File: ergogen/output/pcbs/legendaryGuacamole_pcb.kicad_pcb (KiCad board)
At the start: 2 copper layers, 47 parts

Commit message: forget to commit
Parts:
- removed REF**: XIAO-nRF52840-SMD, XIAO-nRF52840-SMD
- moved S22 215.1 mm to (227.2, 149.6), turned to -40 degrees
- moved D22 214.3 mm to (224.0, 153.5), turned to -40 degrees
- moved S21 209.5 mm to (213.8, 128.7), turned to -30 degrees
- moved D21 208.8 mm to (211.3, 133.0), turned to -30 degrees
- moved S20 207.0 mm to (204.3, 145.2), turned to -30 degrees
- moved D20 206.4 mm to (201.8, 149.5), turned to -30 degrees
- moved S19 201.4 mm to (191.5, 120.1), turned to -20 degrees
- moved D19 201.0 mm to (189.8, 124.8), turned to -20 degrees
- moved S18 200.0 mm to (185.0, 138.0), turned to -20 degrees
- moved D12 200.0 mm to (176.0, 98.7)
- moved D13 200.0 mm to (176.0, 79.7)
- moved D15 200.0 mm to (195.0, 98.7)
- moved D16 200.0 mm to (195.0, 79.7)
- moved D6 200.0 mm to (138.0, 98.7)
- moved D7 200.0 mm to (138.0, 79.7)
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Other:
- net class Default removed

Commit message: final key layout
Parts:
- added D23: , ComboDiode, F.Cu at (222.1, 143.9)
- added REF**: XIAO-nRF52840-SMD, XIAO-nRF52840-SMD, F.Cu at (0.00, 0.00)
- added S23: , MX, F.Cu at (224.6, 139.6)
- moved S18 82.9 mm to (195.0, 55.7), turned to 0 degrees
- moved D18 82.9 mm to (195.0, 60.7), turned to 0 degrees
- moved D12 48.2 mm to (157.0, 54.3)
- moved S12 48.2 mm to (157.0, 49.3)
- moved D15 42.5 mm to (176.0, 60.7)
- moved S15 42.5 mm to (176.0, 55.7)
- moved D3 42.5 mm to (100.0, 67.0)
- moved S3 42.5 mm to (100.0, 62.0)
- moved D6 36.9 mm to (119.0, 67.0)
- moved S6 36.9 mm to (119.0, 62.0)
- moved D9 36.9 mm to (138.0, 60.7)
- moved S9 36.9 mm to (138.0, 55.7)
- moved S20 34.7 mm to (184.3, 116.8), turned to -10 degrees
- moved S22 34.3 mm to (207.7, 121.3), turned to -20 degrees
- moved D20 33.3 mm to (183.4, 121.7), turned to -10 degrees
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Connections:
- D10 pad 1: P7 -> P8
- D10 pad 2: middle_home -> middle_bottom
- D11 pad 1: P6 -> P7
- D11 pad 2: middle_top -> middle_home
- D12 pad 1: P8 -> P6
- D12 pad 2: index_bottom -> middle_top
- D13 pad 1: P7 -> P8
- D13 pad 2: index_home -> index_bottom
- D14 pad 1: P6 -> P7
- D14 pad 2: index_top -> index_home
- D15 pad 1: P8 -> P6
- D15 pad 2: inner_bottom -> index_top
- D16 pad 1: P7 -> P8
- D16 pad 2: inner_home -> inner_bottom
- D17 pad 1: P6 -> P7
- D17 pad 2: inner_top -> inner_home
- D18 pad 1: P10 -> P6
- D18 pad 2: thumb_1_row_0 -> inner_top
- D19 pad 1: P9 -> P10
- D19 pad 2: thumb_1_row_1 -> thumb_1_row_0
- D20 pad 1: P10 -> P9
- D20 pad 2: thumb_2_row_0 -> thumb_1_row_1
- D21 pad 1: P9 -> P10
- D21 pad 2: thumb_2_row_1 -> thumb_2_row_0
- D22 pad 1: P10 -> P9
- D22 pad 2: thumb_3_row_0 -> thumb_2_row_1
- D3 pad 1: P8 -> P6
- D3 pad 2: pinky_bottom -> outer_top
- D4 pad 1: P7 -> P8
- D4 pad 2: pinky_home -> pinky_bottom
- D5 pad 1: P6 -> P7
- D5 pad 2: pinky_top -> pinky_home
- D6 pad 1: P8 -> P6
- D6 pad 2: ring_bottom -> pinky_top
- D7 pad 1: P7 -> P8
- D7 pad 2: ring_home -> ring_bottom
- D8 pad 1: P6 -> P7
- D8 pad 2: ring_top -> ring_home
- D9 pad 1: P8 -> P6
- D9 pad 2: middle_bottom -> ring_top
- S10 pad 2: middle_home -> middle_bottom
- S11 pad 2: middle_top -> middle_home
- S12 pad 1: P4 -> P3
- S12 pad 2: index_bottom -> middle_top
- S13 pad 2: index_home -> index_bottom
- S14 pad 2: index_top -> index_home
- S15 pad 1: P5 -> P4
- S15 pad 2: inner_bottom -> index_top
- S16 pad 2: inner_home -> inner_bottom
- S17 pad 2: inner_top -> inner_home
- S18 pad 1: P3 -> P5
- S18 pad 2: thumb_1_row_0 -> inner_top
- S19 pad 2: thumb_1_row_1 -> thumb_1_row_0
- S20 pad 1: P4 -> P3
- S20 pad 2: thumb_2_row_0 -> thumb_1_row_1
- S21 pad 2: thumb_2_row_1 -> thumb_2_row_0
- S22 pad 1: P5 -> P4
- S22 pad 2: thumb_3_row_0 -> thumb_2_row_1
- S3 pad 1: P1 -> P0
- S3 pad 2: pinky_bottom -> outer_top
- S4 pad 2: pinky_home -> pinky_bottom
- S5 pad 2: pinky_top -> pinky_home
- S6 pad 1: P2 -> P1
- S6 pad 2: ring_bottom -> pinky_top
- S7 pad 2: ring_home -> ring_bottom
- S8 pad 2: ring_top -> ring_home
- S9 pad 1: P3 -> P2
- S9 pad 2: middle_bottom -> ring_top

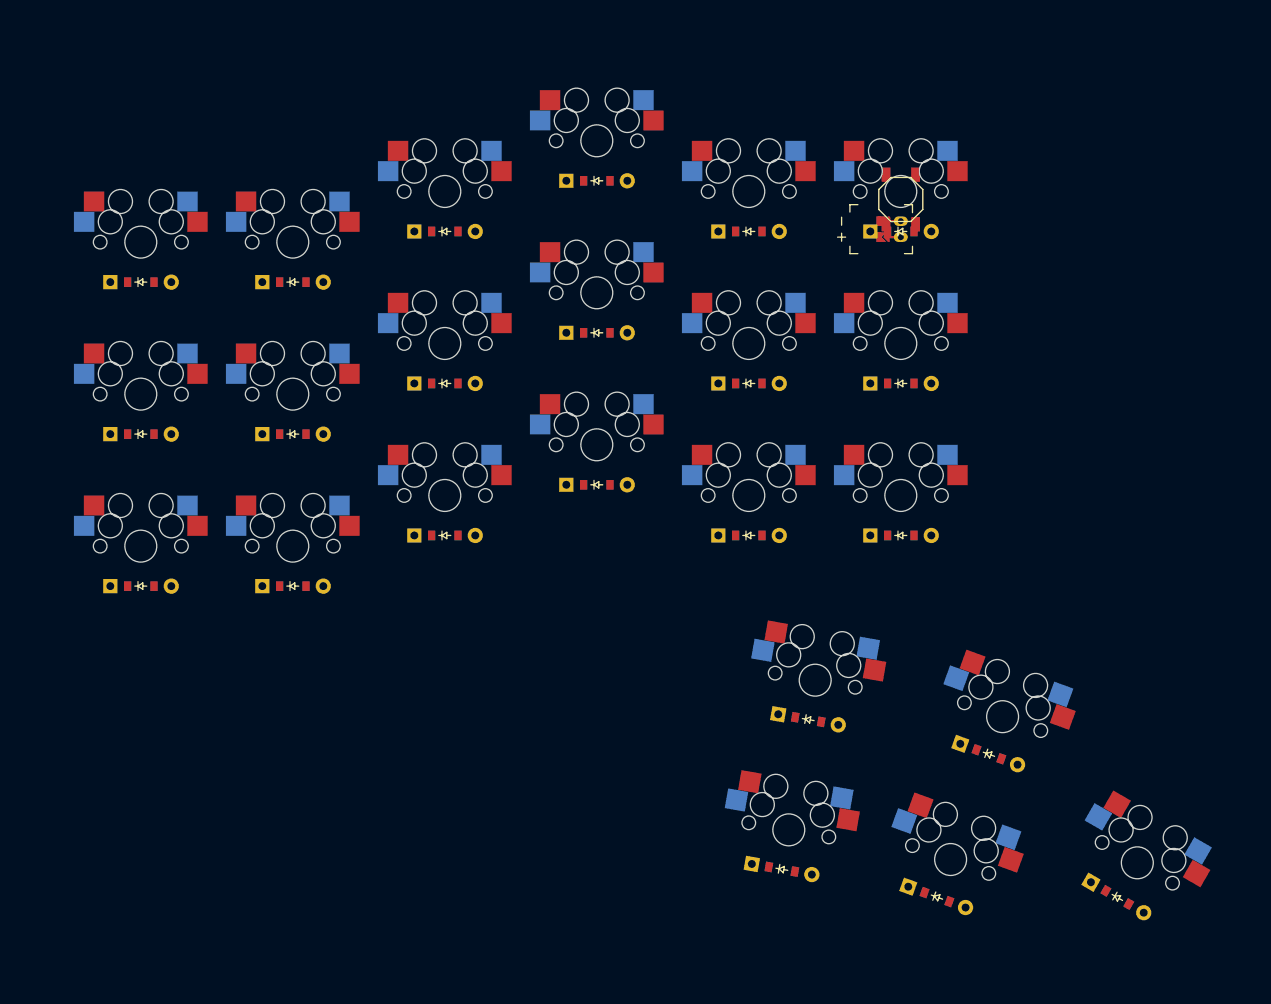
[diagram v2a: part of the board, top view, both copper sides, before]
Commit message: fix pcb (update sw footprint), start case design
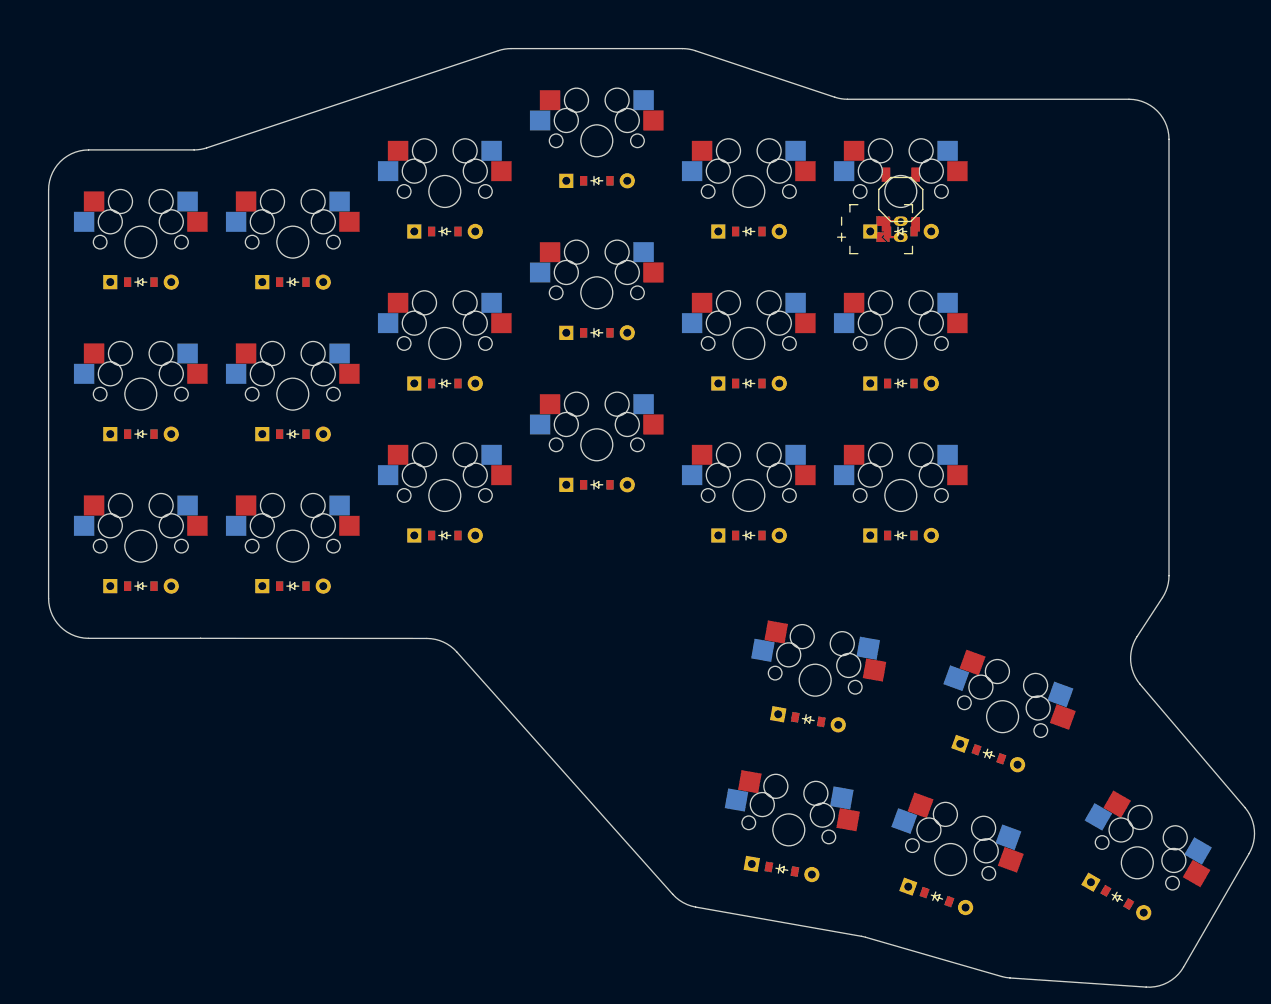
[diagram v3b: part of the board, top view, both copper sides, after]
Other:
- board outline added: 150.7 x 117.3 mm
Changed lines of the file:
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@@
   (title_block
     (title "legendaryGuacamole_pcb")
-    (date "2026-01-21")
+    (date "2026-01-23")
     (rev "v1.0.0")
     (company "Diablica")
@@
     )
   )
+  (gr_line (start 88.475 106.525) (end 88.475 55.475) (layer Edge.Cuts) (stroke (width 0.15) (type default)))
+(gr_line (start 93.475 50.475) (end 106.6636117040513 50.475) (layer Edge.Cuts) (stroke (width 0.15) (type default)))
+(gr_line (start 108.24475068405127 50.21841644000001) (end 144.7052493281026 38.06491685999999) (layer Edge.Cuts) (stroke (width 0.15) (type default)))
+(gr_line (start 146.28638830810263 37.808333299999994) (end 167.71361169189737 37.808333299999994) (layer Edge.Cuts) (stroke (width 0.15) (type default)))
+(gr_line (start 169.29475067189742 38.06491686000001) (end 186.7552493281026 43.88508313999999) (layer Edge.Cuts) (stroke (width 0.15) (type default)))
+(gr_line (start 188.33638830810264 44.14166670000001) (end 223.525 44.14166670000001) (layer Edge.Cuts) (stroke (width 0.15) (type default)))
+(gr_line (start 228.525 49.14166670000001) (end 228.525 103.7046128906315) (layer Edge.Cuts) (stroke (width 0.15) (type default)))
+(gr_line (start 227.71235002139701 106.43702940459406) (end 224.53776635689925 111.30198750768221) (layer Edge.Cuts) (stroke (width 0.15) (type default)))
+(gr_line (start 224.91679732028317 117.27426607099835) (end 238.02377626345938 132.68095847333166) (layer Edge.Cuts) (stroke (width 0.15) (type default)))
+(gr_line (start 238.54558420544618 138.4208205226853) (end 230.34090833802992 152.6317360151316) (layer Edge.Cuts) (stroke (width 0.15) (type default)))
+(gr_line (start 225.67648483180594 155.12054810801365) (end 208.65067101680498 153.9796614916567) (layer Edge.Cuts) (stroke (width 0.15) (type default)))
+(gr_line (start 207.59891348870966 153.7948950177248) (end 190.60432732339262 148.89164919504304) (layer Edge.Cuts) (stroke (width 0.15) (type default)))
+(gr_line (start 190.08651425185596 148.77165602506335) (end 169.35856764628346 145.11675977833818) (layer Edge.Cuts) (stroke (width 0.15) (type default)))
+(gr_line (start 166.4937897641463 143.51906585122265) (end 139.4902371365632 113.21409806628387) (layer Edge.Cuts) (stroke (width 0.15) (type default)))
+(gr_line (start 135.75994829153424 111.54044362809798) (end 107.4762820473352 111.52500069999995) (layer Edge.Cuts) (stroke (width 0.15) (type default)))
+(gr_line (start 107.4735520474444 111.525) (end 93.475 111.525) (layer Edge.Cuts) (stroke (width 0.15) (type default)))
+(gr_arc (start 93.475 50.475) (mid 89.93946609999999 51.939466100000004) (end 88.475 55.475) (layer Edge.Cuts) (stroke (width 0.15) (type default)))
+(gr_arc (start 106.6636117040513 50.475) (mid 107.4645230040513 50.4104373) (end 108.2447507040513 50.2184164) (layer Edge.Cuts) (stroke (width 0.15) (type default)))
+(gr_arc (start 146.28638830810263 37.80833329999999) (mid 145.48547700810263 37.87289599999998) (end 144.70524930810262 38.064916899999986) (layer Edge.Cuts) (stroke (width 0.15) (type default)))
+(gr_arc (start 169.29475069189738 38.06491689999999) (mid 168.51452299189737 37.87289609999999) (end 167.71361169189737 37.808333299999994) (layer Edge.Cuts) (stroke (width 0.15) (type default)))
+(gr_arc (start 186.75524930810263 43.88508310000001) (mid 187.53547700810265 44.07710390000001) (end 188.33638830810264 44.14166670000001) (layer Edge.Cuts) (stroke (width 0.15) (type default)))
+(gr_arc (start 228.525 49.14166670000001) (mid 227.0605339 45.60613280000001) (end 223.525 44.14166670000001) (layer Edge.Cuts) (stroke (width 0.15) (type default)))
+(gr_arc (start 227.71235000000001 106.4370293906315) (mid 228.3175333 105.1299636906315) (end 228.525 103.7046128906315) (layer Edge.Cuts) (stroke (width 0.15) (type default)))
+(gr_arc (start 224.53776637829634 111.30198752164466) (mid 223.73515557829634 114.35109212164465) (end 224.91679737829634 117.27426602164466) (layer Edge.Cuts) (stroke (width 0.15) (type default)))
+(gr_arc (start 238.54558420544618 138.4208205226853) (mid 239.19492300544619 135.4681398226853) (end 238.02377620544618 132.6809585226853) (layer Edge.Cuts) (stroke (width 0.15) (type default)))
+(gr_arc (start 225.67648483802992 155.12054811513164) (mid 228.36454683802992 154.54306101513166) (end 230.34090833802992 152.63173601513165) (layer Edge.Cuts) (stroke (width 0.15) (type default)))
+(gr_arc (start 207.59891352302895 153.79489499877474) (mid 208.11984552302894 153.91543709877473) (end 208.65067102302896 153.97966149877473) (layer Edge.Cuts) (stroke (width 0.15) (type default)))
+(gr_arc (start 190.60432728907335 148.8916492139931) (mid 190.34701638907336 148.8247669139931) (end 190.08651418907334 148.7716561139931) (layer Edge.Cuts) (stroke (width 0.15) (type default)))
+(gr_arc (start 166.4937897090661 143.51906588940847) (mid 167.7914330090661 144.55952138940845) (end 169.35856760906609 145.11675978940846) (layer Edge.Cuts) (stroke (width 0.15) (type default)))
+(gr_arc (start 139.49023719164336 113.21409802809806) (mid 137.80398029164337 111.97856112809806) (end 135.75994829164338 111.54044362809806) (layer Edge.Cuts) (stroke (width 0.15) (type default)))
+(gr_arc (start 107.4762820474444 111.5250007) (mid 107.4749170474444 111.5250001) (end 107.4735520474444 111.525) (layer Edge.Cuts) (stroke (width 0.15) (type default)))
+(gr_arc (start 88.475 106.525) (mid 89.93946609999999 110.06053390000001) (end 93.475 111.525) (layer Edge.Cuts) (stroke (width 0.15) (type default)))
 )
